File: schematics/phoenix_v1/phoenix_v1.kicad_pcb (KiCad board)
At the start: 2 copper layers, 106 x 64.5 mm, 15 parts, among them J1 Screw_Terminal_01x02, J2 Conn_01x09_Socket, SW1 RotaryEncoder_Switch, U1 ESP32-S3-DevKitC, U2 NHD-C0220BIZ

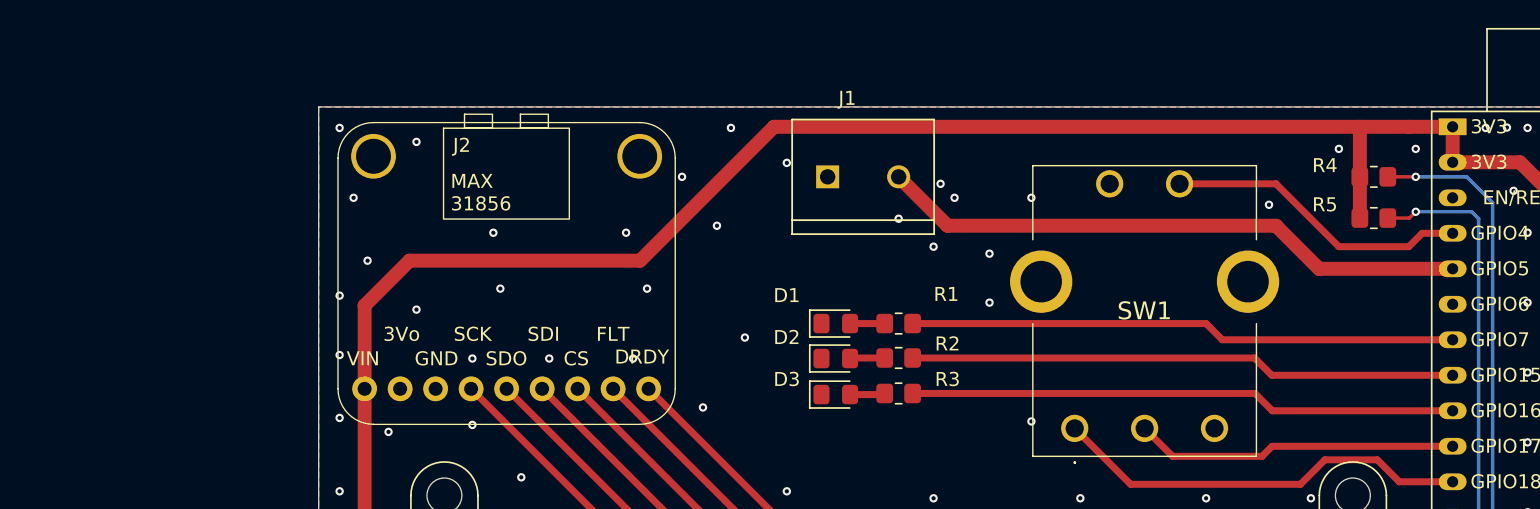
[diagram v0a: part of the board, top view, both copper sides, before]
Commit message: add logo in
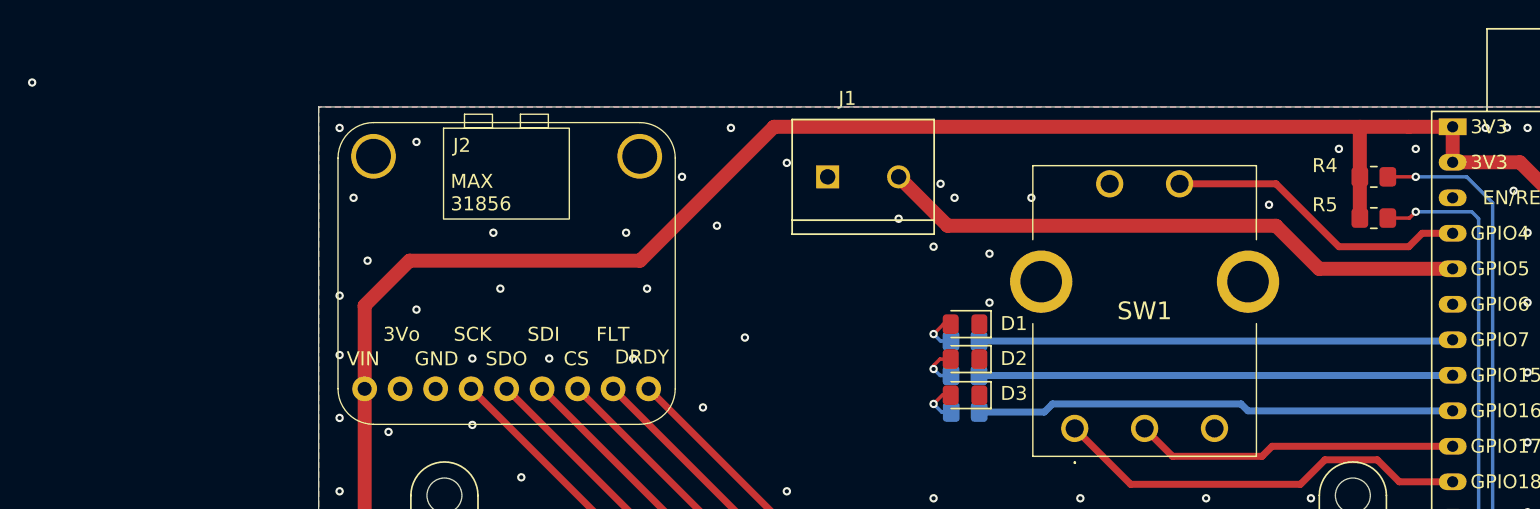
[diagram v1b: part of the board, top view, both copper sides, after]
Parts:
- R1, R2, R3: moved to B.Cu
- moved D1 9.25 mm to (130.2, 74.0), turned to 180 degrees
- moved D2 9.25 mm to (130.2, 76.5), turned to 180 degrees
- moved D3 9.25 mm to (130.2, 79.1), turned to 180 degrees
- moved R3 4.95 mm to (130.3, 80.3)
- moved R1 4.91 mm to (130.2, 75.2)
- moved R2 4.91 mm to (130.2, 77.7)
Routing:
- net /LED_2: track 39.2 -> 33.9 mm
- net /LED_1: track 39.1 -> 33.9 mm
- net /LED_3: track 39.2 -> 34.3 mm
- net Net-(D2-A): track 2.49 -> 3.37 mm, vias 0 -> 1
- net Net-(D1-A): track 2.47 -> 2.98 mm, vias 0 -> 1
- net Net-(D3-A): track 2.51 -> 2.99 mm, vias 0 -> 1
- net GND: vias 128 -> 127
- net (no net): vias 0 -> 1

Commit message: hf logo as footprint
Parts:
- added G***: LOGO, !footprints:HF_logo, F.Cu at (119.0, 79.0)

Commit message: add names and mounting holes
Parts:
- added REF**: MountingHole_2.2mm_M2, MountingHole:MountingHole_2.2mm_M2, F.Cu at (192.0, 120.0)
- added REF**: MountingHole_2.2mm_M2, MountingHole:MountingHole_2.2mm_M2, F.Cu at (81.5, 61.5)
- added REF**: MountingHole_2.2mm_M2, MountingHole:MountingHole_2.2mm_M2, F.Cu at (81.5, 120.0)
- added REF**: MountingHole_2.2mm_M2, MountingHole:MountingHole_2.2mm_M2, F.Cu at (192.0, 61.5)
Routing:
- net GND: vias 127 -> 143
- net (no net): vias 1 -> 0
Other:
- board size 106 x 64.5 mm -> 116.5 x 64.5 mm
- board text added: "Akmatbek Suleimanov, Edward Wang, Maria Nastase - April 2025"
- board text added: "JLCJLCJLCJLC"
